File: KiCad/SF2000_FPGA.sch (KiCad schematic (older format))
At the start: 21 parts, among them J10 Conn_02x01, J11 Conn_02x01, J3 Conn_02x05_Odd_Even, J4 Conn_02x01, J8 Conn_02x01, J9 Conn_02x01, U20 AT25SF081B-SSH, U28 GW1N-UV9LQ144, U8 T8Q144C3

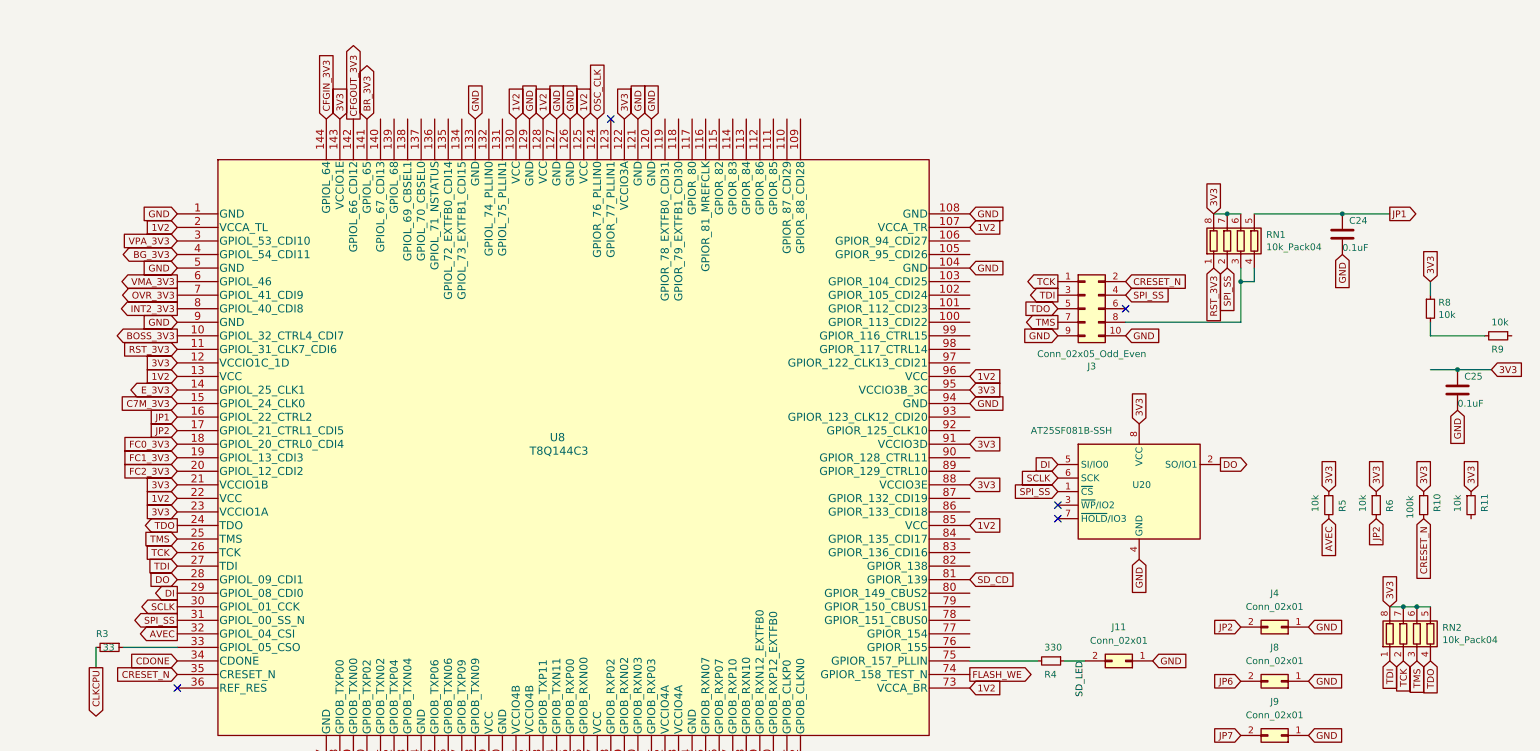
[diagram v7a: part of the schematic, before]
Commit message: Add INT6 signal, Move RN5 to SF2000_FPGA sheet
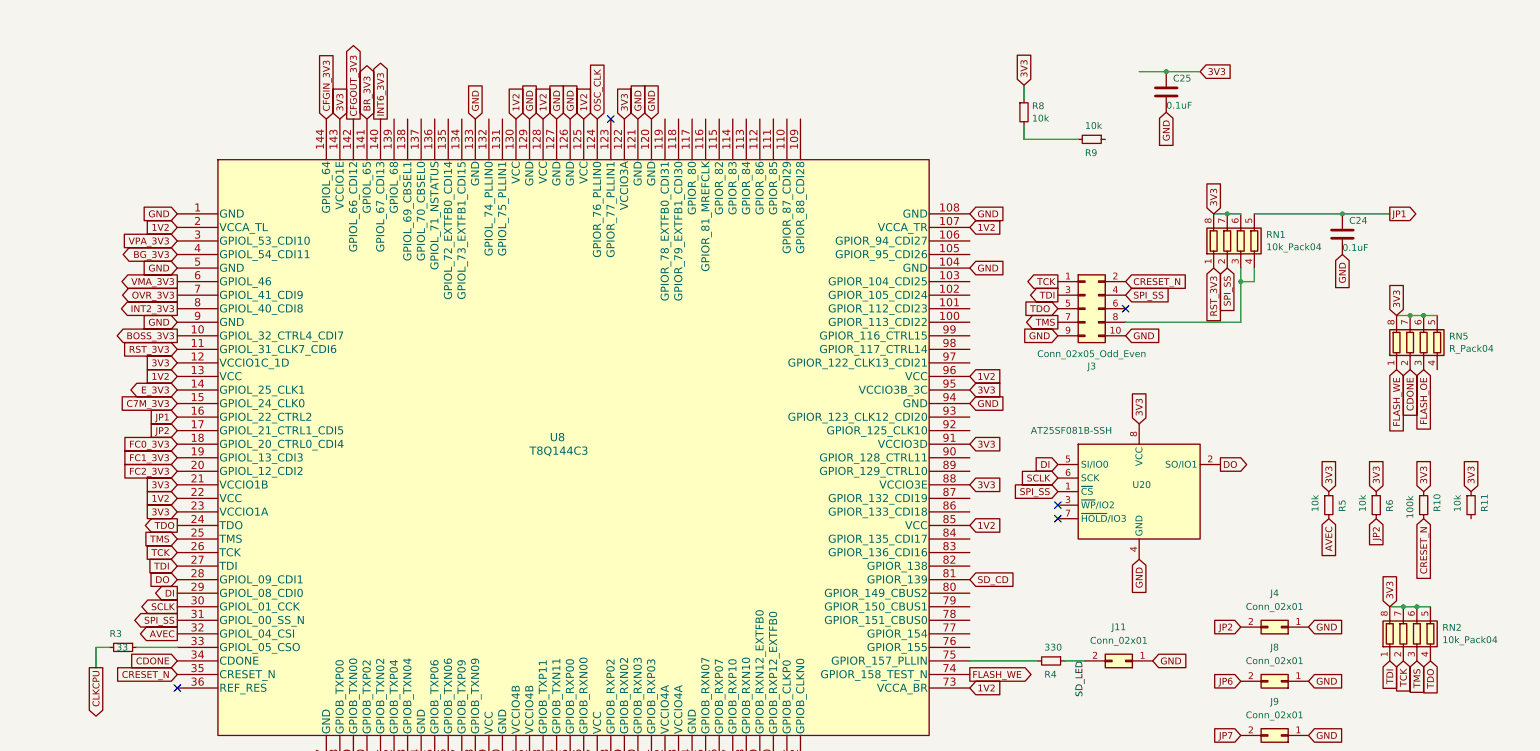
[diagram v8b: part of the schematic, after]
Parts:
- added RN5: R_Pack04, SF2000:RESCAF80P320X160X60-8N, symbol Device:R_Pack04
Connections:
- net 3V3: now also RN5.5 (R4.2), RN5.6 (R3.2), RN5.7 (R2.2), RN5.8 (R1.2)
- net CDONE: now also RN5.2 (R2.1)
- net FLASH_OE: now also RN5.3 (R3.1)
- net FLASH_WE: now also RN5.1 (R1.1)
- net INT6_3V3: now reaches U8.140 (GPIOL_67_CDI13)
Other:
- moved on the sheet: C25, R3, R8, R9
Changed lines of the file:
@@
 Wire Wire Line
 	10350 4700 10450 4700
-Text GLabel 10450 2300 1    50   Input ~ 0
+Text GLabel 7450 850  1    50   Input ~ 0
 3V3
 $Comp
@@
 Text GLabel 9800 2100 3    50   Input ~ 0
 GND
-Text GLabel 10900 2950 2    50   Input ~ 0
+Text GLabel 8750 750  2    50   Input ~ 0
 3V3
 Wire Wire Line
@@
 L Device:C C?
 U 1 1 624B4CFC
-P 10650 3100
+P 8500 900
 AR Path="/624B4CFC" Ref="C?"  Part="1"
 AR Path="/620D263D/624B4CFC" Ref="C25"  Part="1"
-F 0 "C25" H 10700 3200 50  0000 L CNN
-F 1 "0.1uF" H 10650 3000 50  0000 L CNN
-F 2 "Capacitor_SMD:C_0805_2012Metric_Pad1.15x1.40mm_HandSolder" H 10688 2950 50  0001 C CNN
-F 3 "~" H 10650 3100 50  0001 C CNN
-	1    10650 3100
-	1    0    0    -1
-$EndComp
-Text GLabel 10650 3250 3    50   Input ~ 0
-GND
-Wire Wire Line
-	10450 2950 10650 2950
-Connection ~ 10650 2950
-Wire Wire Line
-	10650 2950 10900 2950
+F 0 "C25" H 8550 1000 50  0000 L CNN
+F 1 "0.1uF" H 8500 800 50  0000 L CNN
+F 2 "Capacitor_SMD:C_0805_2012Metric_Pad1.15x1.40mm_HandSolder" H 8538 750 50  0001 C CNN
+F 3 "~" H 8500 900 50  0001 C CNN
+	1    8500 900
+	1    0    0    -1
+$EndComp
+Text GLabel 8500 1050 3    50   Input ~ 0
+GND
+Wire Wire Line
+	8300 750  8500 750
+Connection ~ 8500 750
+Wire Wire Line
+	8500 750  8750 750
 $Comp
 L Device:R_Small R?
 U 1 1 62517BB4
-P 10450 2500
+P 7450 1050
 AR Path="/62517BB4" Ref="R?"  Part="1"
 AR Path="/620D263D/62517BB4" Ref="R8"  Part="1"
-F 0 "R8" H 10509 2546 50  0000 L CNN
-F 1 "10k" H 10509 2455 50  0000 L CNN
-F 2 "Resistor_SMD:R_0805_2012Metric_Pad1.15x1.40mm_HandSolder" H 10450 2500 50  0001 C CNN
-F 3 "~" H 10450 2500 50  0001 C CNN
-	1    10450 2500
+F 0 "R8" H 7509 1096 50  0000 L CNN
+F 1 "10k" H 7509 1005 50  0000 L CNN
+F 2 "Resistor_SMD:R_0805_2012Metric_Pad1.15x1.40mm_HandSolder" H 7450 1050 50  0001 C CNN
+F 3 "~" H 7450 1050 50  0001 C CNN
+	1    7450 1050
 	1    0    0    -1
 $EndComp
@@
 L Device:R_Small R?
 U 1 1 62519236
-P 10950 2700
+P 7950 1250
 AR Path="/62519236" Ref="R?"  Part="1"
 AR Path="/620D263D/62519236" Ref="R9"  Part="1"
-F 0 "R9" V 11050 2650 50  0000 L CNN
-F 1 "10k" V 10850 2650 50  0000 L CNN
-F 2 "Resistor_SMD:R_0805_2012Metric_Pad1.15x1.40mm_HandSolder" H 10950 2700 50  0001 C CNN
-F 3 "~" H 10950 2700 50  0001 C CNN
-	1    10950 2700
+F 0 "R9" V 8050 1200 50  0000 L CNN
+F 1 "10k" V 7850 1200 50  0000 L CNN
+F 2 "Resistor_SMD:R_0805_2012Metric_Pad1.15x1.40mm_HandSolder" H 7950 1250 50  0001 C CNN
+F 3 "~" H 7950 1250 50  0001 C CNN
+	1    7950 1250
 	0    1    1    0
 $EndComp
 Wire Wire Line
-	10450 2400 10450 2300
-Wire Wire Line
-	10450 2600 10450 2700
-Wire Wire Line
-	10850 2700 10450 2700
+	7450 950  7450 850
+Wire Wire Line
+	7450 1150 7450 1250
+Wire Wire Line
+	7850 1250 7450 1250
 Connection ~ 9800 1800
 $Comp
@@
 L Device:R_Small R?
 U 1 1 6302BBCE
-P 700 5000
+P 800 5000
 AR Path="/6302BBCE" Ref="R?"  Part="1"
 AR Path="/620D263D/6302BBCE" Ref="R3"  Part="1"
-F 0 "R3" V 600 4900 50  0000 L CNN
-F 1 "33" V 700 4950 50  0000 L CNN
-F 2 "Resistor_SMD:R_0805_2012Metric_Pad1.15x1.40mm_HandSolder" H 700 5000 50  0001 C CNN
-F 3 "~" H 700 5000 50  0001 C CNN
-	1    700  5000
+F 0 "R3" V 700 4900 50  0000 L CNN
+F 1 "33" V 800 4950 50  0000 L CNN
+F 2 "Resistor_SMD:R_0805_2012Metric_Pad1.15x1.40mm_HandSolder" H 800 5000 50  0001 C CNN
+F 3 "~" H 800 5000 50  0001 C CNN
+	1    800  5000
 	0    1    1    0
 $EndComp
@@
 SCLK
 Wire Wire Line
-	1200 5000 800  5000
-Wire Wire Line
 	600  5000 600  5150
 Text GLabel 8950 2200 3    50   Input ~ 0
@@
 Text GLabel 9700 4050 3    50   Input ~ 0
 AVEC
+Text GLabel 2700 1100 1    50   Output ~ 0
+INT6_3V3
+Wire Wire Line
+	900  5000 1200 5000
+Wire Wire Line
+	700  5000 600  5000
+Text GLabel 10200 2550 1    50   Input ~ 0
+3V3
+$Comp
+L Device:R_Pack04 RN?
+U 1 1 67FCD62D
+P 10400 2750
+AR Path="/62892CF3/67FCD62D" Ref="RN?"  Part="1"
+AR Path="/621DFEC4/67FCD62D" Ref="RN?"  Part="1"
+AR Path="/620D263D/67FCD62D" Ref="RN5"  Part="1"
+F 0 "RN5" H 10588 2796 50  0000 L CNN
+F 1 "R_Pack04" H 10588 2705 50  0000 L CNN
+F 2 "SF2000:RESCAF80P320X160X60-8N" V 10675 2750 50  0001 C CNN
+F 3 "~" H 10400 2750 50  0001 C CNN
+	1    10400 2750
+	1    0    0    -1
+$EndComp
+Wire Wire Line
+	10200 2550 10300 2550
+Connection ~ 10300 2550
+Wire Wire Line
+	10300 2550 10400 2550
+Connection ~ 10400 2550
+Wire Wire Line
+	10400 2550 10500 2550
+Text GLabel 10300 2950 3    50   Input ~ 0
+CDONE
+Text GLabel 10200 2950 3    50   Input ~ 0
+FLASH_WE
+Text GLabel 10400 2950 3    50   Input ~ 0
+FLASH_OE
 $EndSCHEMATC
